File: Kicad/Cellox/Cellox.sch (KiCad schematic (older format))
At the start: 8 parts

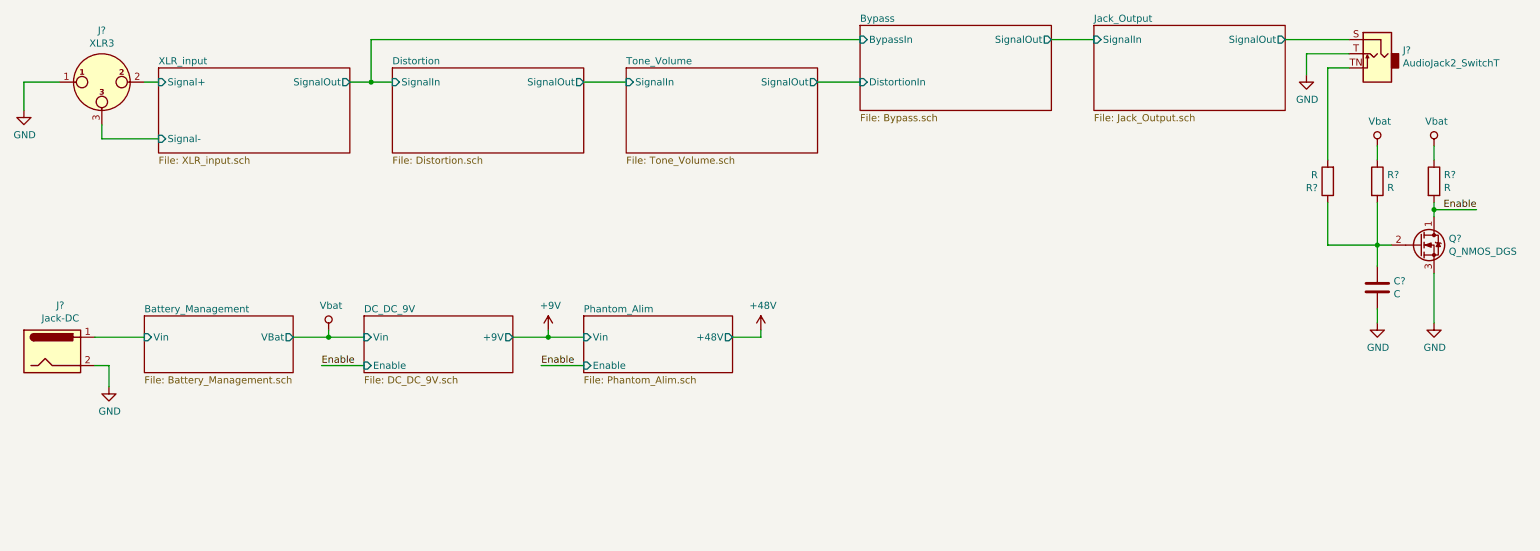
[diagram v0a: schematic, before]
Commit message: Add input stage + clipping stage
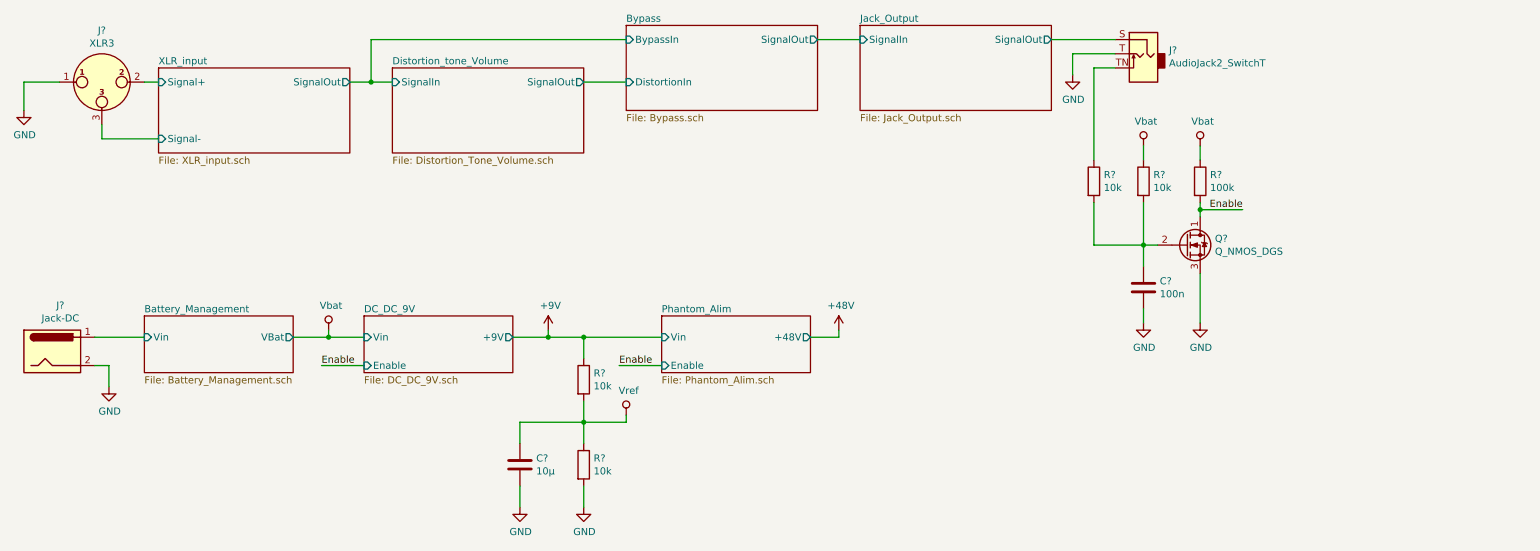
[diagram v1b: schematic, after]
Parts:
- added C?: 10µ, symbol Device:C
- added R? (x2): 10k, symbol Device:R
- C?: value C -> 100n
- R?: value R -> 100k
- R? (x2): value R -> 10k
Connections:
- net +9V: now also R?.1
- net GND: now also C?.2, R?.2
- net at J?.TN: now also R?.1; no longer R?.2
- net at C?.1, Q?.2 (G), R?.2: now also R?.2; no longer R?.1
- new net Vref: C?.1, R?.1, R?.2
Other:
- moved on the sheet: C?, J?, Q?, R?
